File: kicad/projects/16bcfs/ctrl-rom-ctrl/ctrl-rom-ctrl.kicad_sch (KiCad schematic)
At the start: 68 parts, among them J1 Instruction, J2 Control ROM Address, J3 Raw Address for Pgm ROM, J4 Signal Header, J5 Power, J6 Power, U1 74HC08, U11 74HC157, U12 74HC157, U13 74HC157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

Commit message: Look at the MAX704 uProcessor Supervisor
This commit adds the documentation for the MAX704 supervisor.  Some
minor update in teh Control Rom Control circuit are added as well.

Closes #198
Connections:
- net VCC: now also U2.13 (~{R}); no longer U2.10 (~{S})
- net ~{RESET}: now also U2.10 (~{S}); no longer U2.13 (~{R})
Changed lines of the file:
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@@
     (stroke (width 0) (type default))
   )
+  (wire (pts (xy 276.86 316.23) (xy 306.07 316.23))
+    (stroke (width 0) (type default))
+  )
   (wire (pts (xy 36.195 82.55) (xy 36.195 84.455))
     (stroke (width 0) (type default))
@@
     (stroke (width 0) (type default))
   )
+  (wire (pts (xy 276.86 293.37) (xy 276.86 316.23))
+    (stroke (width 0) (type default))
+  )
   (wire (pts (xy 61.595 156.845) (xy 65.405 156.845))
     (stroke (width 0) (type default))
@@
     )
   )
-  (global_label "~{RESET}" (shape input) (at 306.07 316.23 270) (fields_autoplaced)
-    (effects (font (size 1.27 1.27)) (justify right))
-    (property "Intersheetrefs" "${INTERSHEET_REFS}" (at 306.07 324.9603 90)
-      (effects (font (size 1.27 1.27)) (justify right) hide)
+  (global_label "~{RESET}" (shape input) (at 306.07 293.37 90) (fields_autoplaced)
+    (effects (font (size 1.27 1.27)) (justify left))
+    (property "Intersheetrefs" "${INTERSHEET_REFS}" (at 306.07 284.6397 90)
+      (effects (font (size 1.27 1.27)) (justify left) hide)
     )
   )
@@
     )
   )
-  (symbol (lib_id "power:VCC") (at 306.07 293.37 0) (unit 1)
+  (symbol (lib_id "power:VCC") (at 276.86 293.37 0) (unit 1)
     (in_bom yes) (on_board yes) (dnp no) (fields_autoplaced)
-    (property "Reference" "#PWR033" (at 306.07 297.18 0)
+    (property "Reference" "#PWR033" (at 276.86 297.18 0)
       (effects (font (size 1.27 1.27)) hide)
     )
-    (property "Value" "VCC" (at 306.07 288.925 0)
+    (property "Value" "VCC" (at 276.86 288.925 0)
       (effects (font (size 1.27 1.27)))
     )
-    (property "Footprint" "" (at 306.07 293.37 0)
+    (property "Footprint" "" (at 276.86 293.37 0)
       (effects (font (size 1.27 1.27)) hide)
     )
-    (property "Datasheet" "" (at 306.07 293.37 0)
+    (property "Datasheet" "" (at 276.86 293.37 0)
       (effects (font (size 1.27 1.27)) hide)
     )

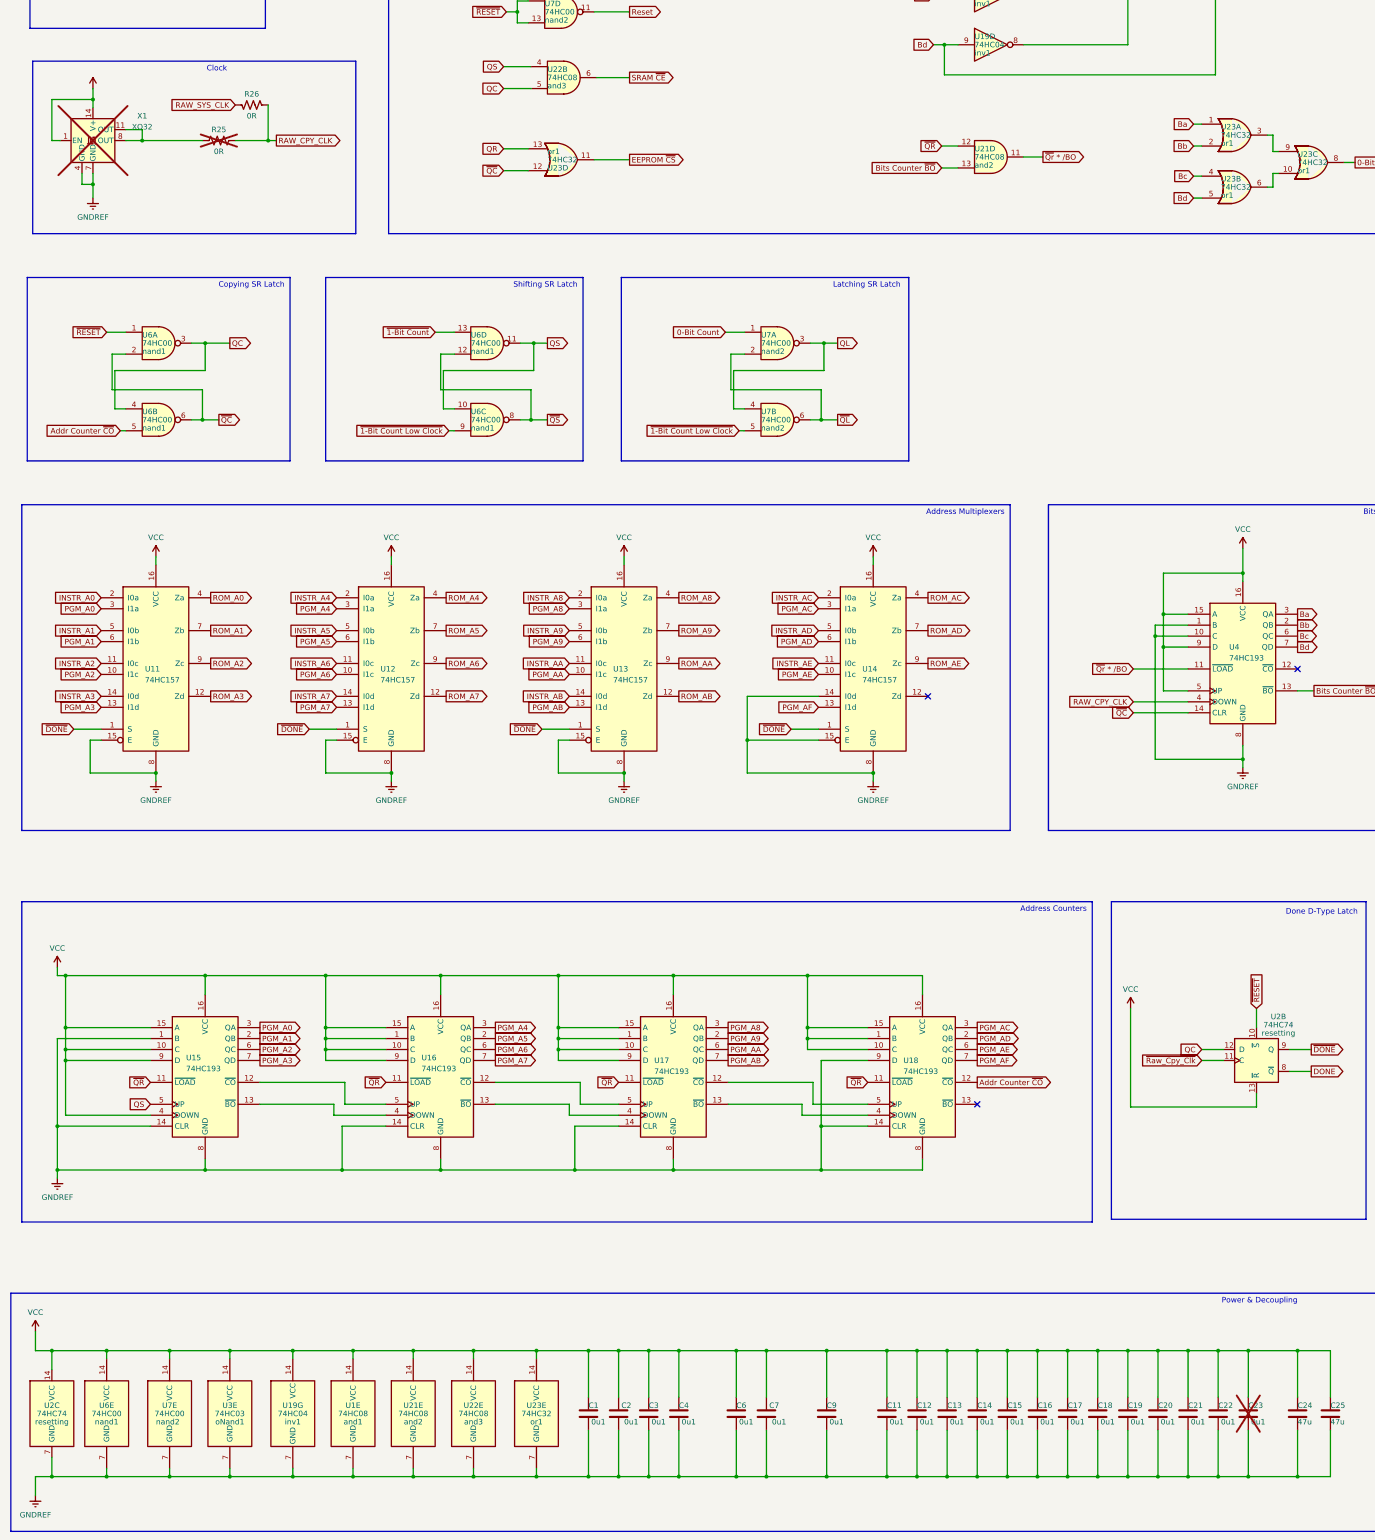
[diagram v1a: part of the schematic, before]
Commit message: Schematic changes for clock and control ROM
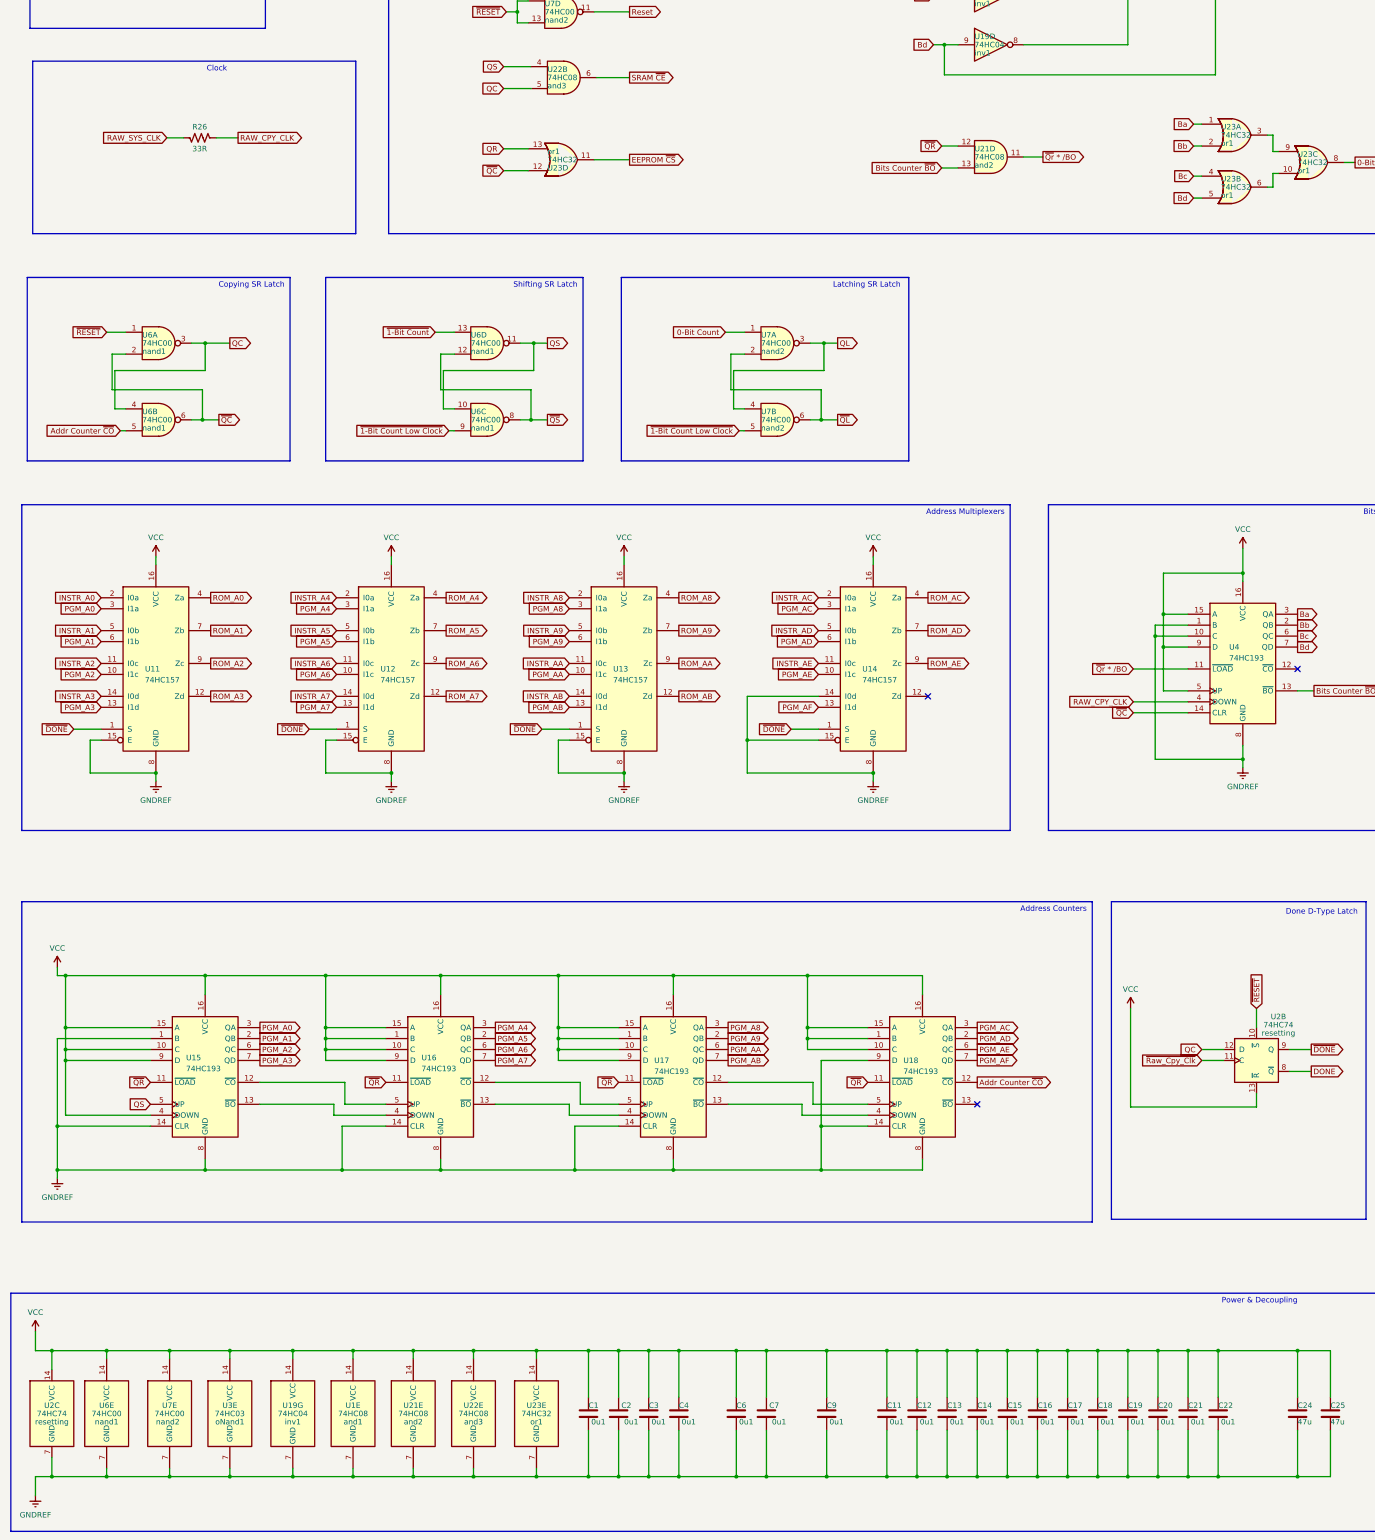
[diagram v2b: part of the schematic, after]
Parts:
- removed C23: 0u1, Capacitor_SMD:C_1206_3216Metric_Pad1.33x1.80mm_HandSolder, symbol Device:C
- removed R25: 0R, Resistor_SMD:R_1206_3216Metric_Pad1.30x1.75mm_HandSolder, symbol Device:R_US
- removed X1: XO32, eryjus:Oscillator_DIP-8-14, symbol eryjus:XO32-Dual
- R26: value 0R -> 33R
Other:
- moved on the sheet: R26
